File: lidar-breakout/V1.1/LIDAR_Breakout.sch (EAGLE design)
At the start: 88 parts, among them J1 UX60-MB-5S8, P1 MOLEX 0436500200, X1 TSX-3225 16.0000MF18X-AC0

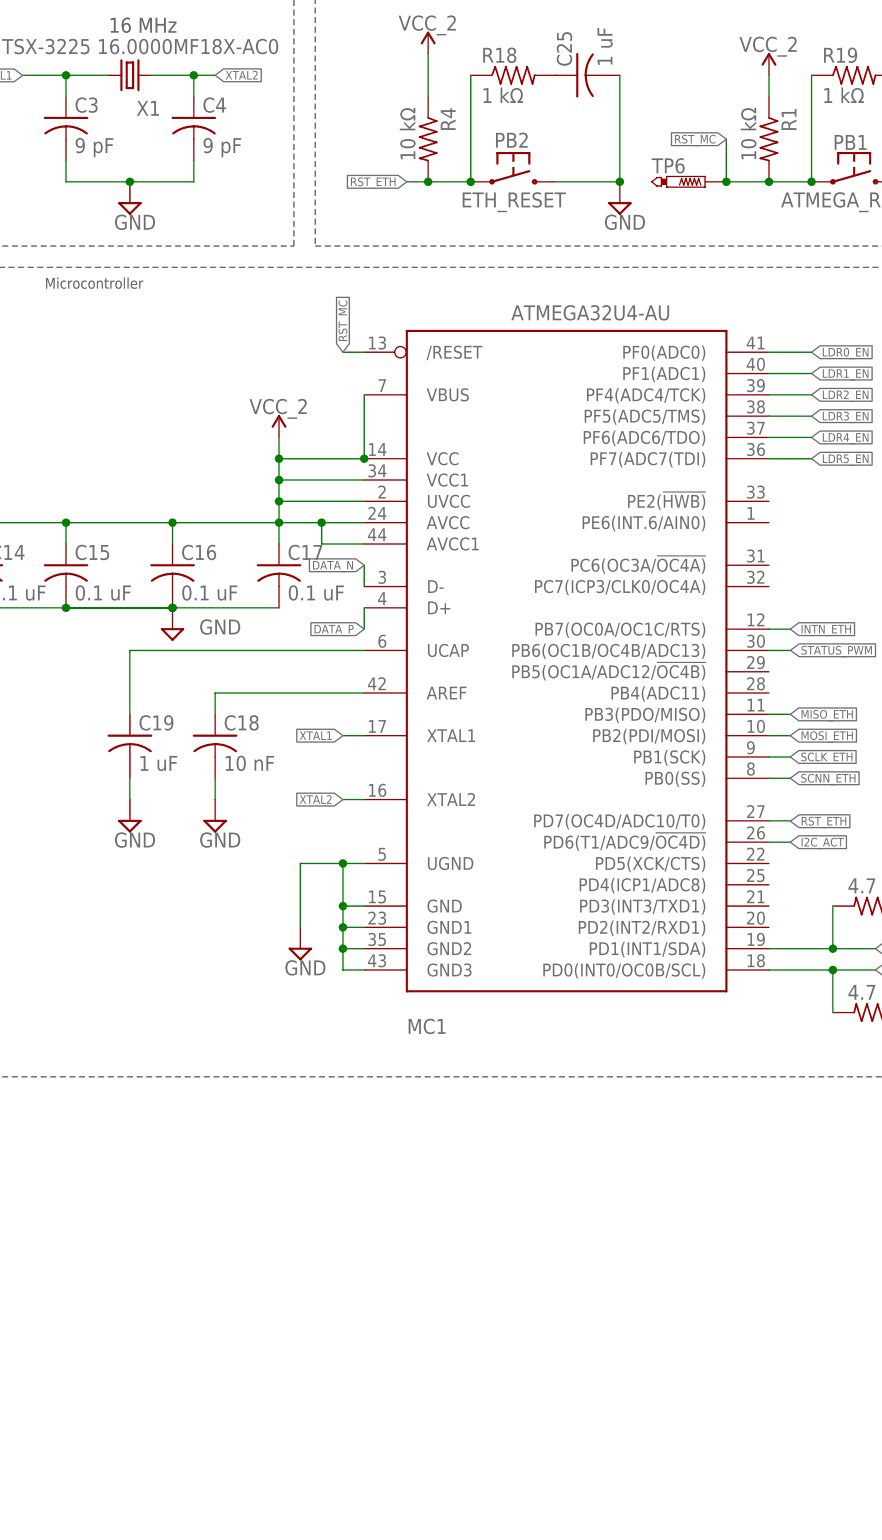
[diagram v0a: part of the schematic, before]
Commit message: Added POGO Pads
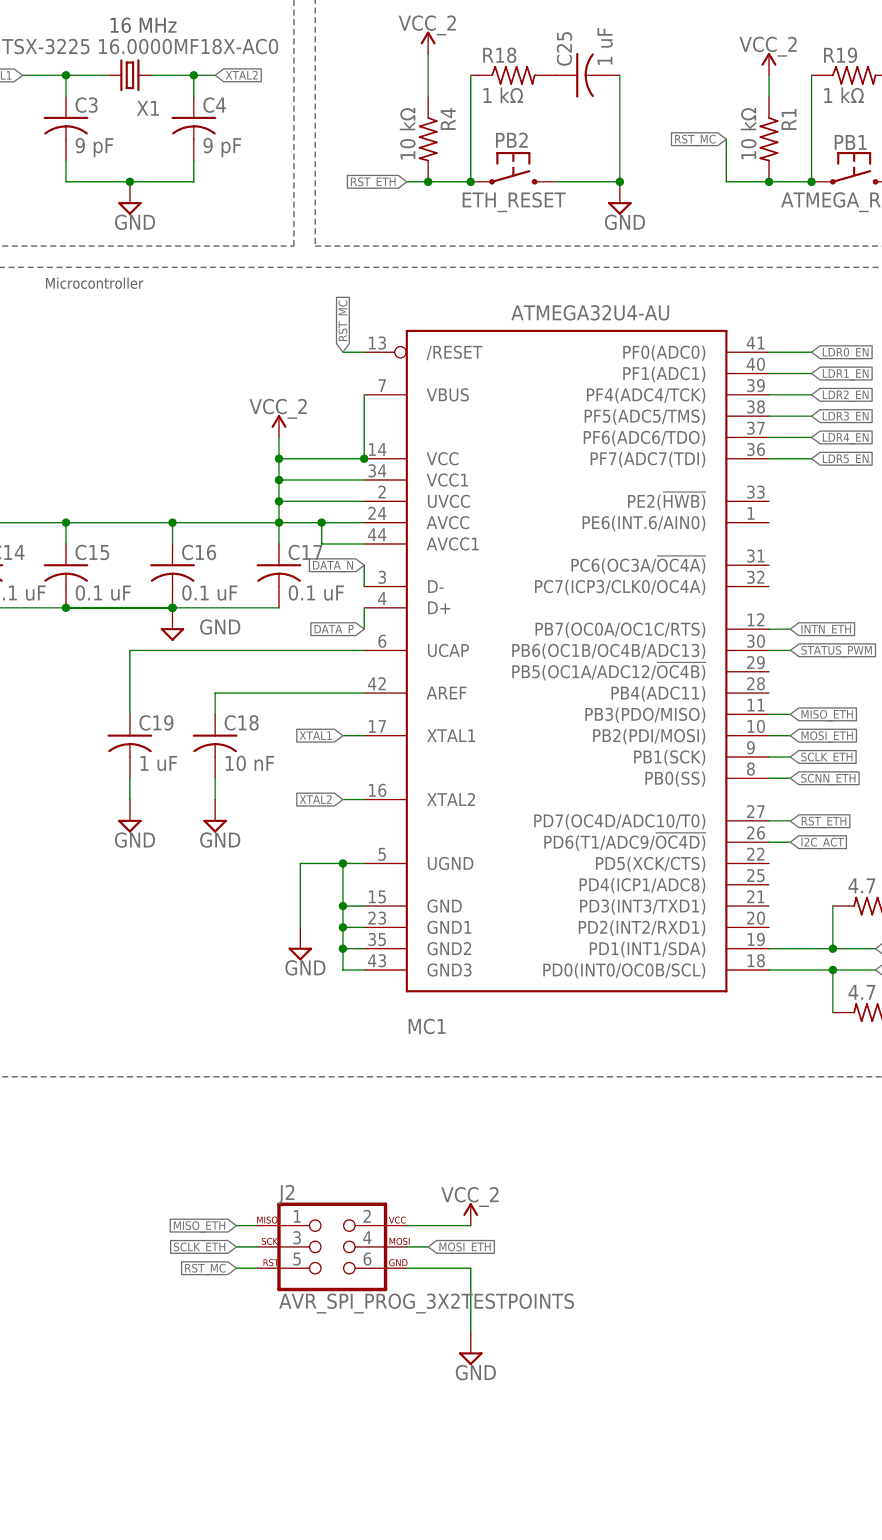
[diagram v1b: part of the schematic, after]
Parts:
- removed TP6: PTR1PAD1-13, testpad:PTR1PAD1-13
- added J2: AVR_SPI_PROG_3X2TESTPOINTS, SparkFun-Connectors:AVR_SPI_PROG_3X2TESTPOINTS
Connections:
- net GND: now also J2.6
- net MISO_ETH: now also J2.1
- net MOSI_ETH: now also J2.4
- net RST_MC: now also J2.5; no longer TP6.TP
- net SCLK_ETH: now also J2.3
- net VCC_2: now also J2.2
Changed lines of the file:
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@@
 <?xml version="1.0" encoding="utf-8"?>
 <!DOCTYPE eagle SYSTEM "eagle.dtd">
-<eagle version="9.3.0">
+<eagle version="9.2.2">
 <drawing>
 <settings>
@@
 <part name="C25" library="resistor" library_urn="urn:adsk.eagle:library:348" deviceset="C-US" device="C0603" package3d_urn="urn:adsk.eagle:package:26138/1" value="1 uF"/>
 <part name="C26" library="resistor" library_urn="urn:adsk.eagle:library:348" deviceset="C-US" device="C0603" package3d_urn="urn:adsk.eagle:package:26138/1" value="0.1 uF"/>
-<part name="TP6" library="testpad" library_urn="urn:adsk.eagle:library:385" deviceset="PTR1" device="PAD1-13" package3d_urn="urn:adsk.eagle:package:27946/1" value="PTR1PAD1-13"/>
 <part name="H1" library="RoboJackets-Connectors" deviceset="SM06B-GHS" device=""/>
 <part name="H2" library="RoboJackets-Connectors" deviceset="SM06B-GHS" device=""/>
@@
 <part name="R18" library="rcl" library_urn="urn:adsk.eagle:library:334" deviceset="R-US_" device="R0603" package3d_urn="urn:adsk.eagle:package:23555/2" value="1 kΩ"/>
 <part name="R19" library="rcl" library_urn="urn:adsk.eagle:library:334" deviceset="R-US_" device="R0603" package3d_urn="urn:adsk.eagle:package:23555/2" value="1 kΩ"/>
+<part name="J2" library="SparkFun-Connectors" library_urn="urn:adsk.eagle:library:513" deviceset="AVR_SPI_PROG_3X2" device="TESTPOINTS" package3d_urn="urn:adsk.eagle:package:38008/1" value="AVR_SPI_PROG_3X2TESTPOINTS"/>
+<part name="SUPPLY14" library="supply2" library_urn="urn:adsk.eagle:library:372" deviceset="GND" device=""/>
+<part name="SUPPLY22" library="SparkFun-PowerSymbols" library_urn="urn:adsk.eagle:library:530" deviceset="VCC_2" device=""/>
 </parts>
 <sheets>
@@
 <attribute name="VALUE" x="258.191" y="244.856" size="1.778" layer="96" rot="R90"/>
 </instance>
-<instance part="TP6" gate="G$1" x="228.6" y="231.14" smashed="yes" rot="R270">
-<attribute name="NAME" x="222.25" y="232.156" size="1.778" layer="95"/>
-<attribute name="TP_SIGNAL_NAME" x="226.06" y="229.87" size="1.778" layer="97" rot="R270"/>
-</instance>
 <instance part="H1" gate="G$1" x="302.26" y="152.4" smashed="yes" rot="MR0">
 <attribute name="NAME" x="307.34" y="170.18" size="1.778" layer="95" font="vector" rot="MR0" align="top-left"/>
@@
 <attribute name="NAME" x="242.57" y="245.3386" size="1.778" layer="95"/>
 <attribute name="VALUE" x="242.57" y="240.538" size="1.778" layer="96"/>
+</instance>
+<instance part="J2" gate="G$1" x="182.88" y="104.14" smashed="yes">
+<attribute name="NAME" x="177.8" y="109.728" size="1.778" layer="95" font="vector"/>
+<attribute name="VALUE" x="177.8" y="96.774" size="1.778" layer="96" font="vector"/>
+</instance>
+<instance part="SUPPLY14" gate="GND" x="200.66" y="91.44" smashed="yes">
+<attribute name="VALUE" x="198.755" y="88.265" size="1.778" layer="96"/>
+</instance>
+<instance part="SUPPLY22" gate="G$1" x="200.66" y="106.68" smashed="yes">
+<attribute name="VALUE" x="200.66" y="109.474" size="1.778" layer="96" align="bottom-center"/>
 </instance>
 </instances>
@@
 <junction x="292.1" y="193.04"/>
 </segment>
+<segment>
+<pinref part="J2" gate="G$1" pin="6"/>
+<wire x1="193.04" y1="101.6" x2="200.66" y2="101.6" width="0.1524" layer="91"/>
+<pinref part="SUPPLY14" gate="GND" pin="GND"/>
+<wire x1="200.66" y1="101.6" x2="200.66" y2="93.98" width="0.1524" layer="91"/>
+</segment>
 </net>
 <net name="RST_MC" class="0">
@@
 <wire x1="231.14" y1="231.14" x2="236.22" y2="231.14" width="0.1524" layer="91"/>
 <junction x="236.22" y="231.14"/>
-<pinref part="TP6" gate="G$1" pin="TP"/>
-<junction x="231.14" y="231.14"/>
 <wire x1="241.3" y1="231.14" x2="241.3" y2="243.84" width="0.1524" layer="91"/>
 <junction x="241.3" y="231.14"/>
@@
 <wire x1="187.96" y1="210.82" x2="185.42" y2="210.82" width="0.1524" layer="91"/>
 <label x="185.42" y="210.82" size="1.016" layer="95" rot="R90" xref="yes"/>
+</segment>
+<segment>
+<pinref part="J2" gate="G$1" pin="5"/>
+<wire x1="175.26" y1="101.6" x2="172.72" y2="101.6" width="0.1524" layer="91"/>
+<label x="172.72" y="101.6" size="1.016" layer="95" rot="R180" xref="yes"/>
 </segment>
 </net>
@@
 <label x="238.76" y="165.1" size="1.016" layer="95" xref="yes"/>
 </segment>
+<segment>
+<pinref part="J2" gate="G$1" pin="4"/>
+<wire x1="193.04" y1="104.14" x2="195.58" y2="104.14" width="0.1524" layer="91"/>
+<label x="195.58" y="104.14" size="1.016" layer="95" xref="yes"/>
+</segment>
 </net>
 <net name="MISO_ETH" class="0">
@@
 <wire x1="236.22" y1="167.64" x2="238.76" y2="167.64" width="0.1524" layer="91"/>
 <label x="238.76" y="167.64" size="1.016" layer="95" xref="yes"/>
+</segment>
+<segment>
+<pinref part="J2" gate="G$1" pin="1"/>
+<wire x1="175.26" y1="106.68" x2="172.72" y2="106.68" width="0.1524" layer="91"/>
+<label x="172.72" y="106.68" size="1.016" layer="95" rot="R180" xref="yes"/>
 </segment>
 </net>
@@
 <pinref part="SUPPLY9" gate="G$1" pin="VCC_2"/>
 </segment>
+<segment>
+<pinref part="J2" gate="G$1" pin="2"/>
+<wire x1="193.04" y1="106.68" x2="200.66" y2="106.68" width="0.1524" layer="91"/>
+<pinref part="SUPPLY22" gate="G$1" pin="VCC_2"/>
+</segment>
 </net>
 <net name="STATUS_PWM" class="0">
@@
 <label x="238.76" y="162.56" size="1.016" layer="95" xref="yes"/>
 </segment>
-</net>
+<segment>
+<pinref part="J2" gate="G$1" pin="3"/>
+<wire x1="175.26" y1="104.14" x2="172.72" y2="104.14" width="0.1524" layer="91"/>
+<label x="172.72" y="104.14" size="1.016" layer="95" rot="R180" xref="yes"/>
+</segment>
+</net>

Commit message: Updated Reset PB
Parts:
- PB1: device RoboJackets-Switches:RESET_PB_RA -> RoboJackets-Switches:PB_RA
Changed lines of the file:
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@@
 <part name="C12" library="resistor" library_urn="urn:adsk.eagle:library:348" deviceset="C-US" device="C0603" package3d_urn="urn:adsk.eagle:package:26138/1" value="0.1 uF"/>
 <part name="C13" library="680uF_Elect_Cap" deviceset="EEE-FTJ681XAP" device="" value="680 uF"/>
-<part name="PB1" library="RoboJackets-Switches" deviceset="RESET_PB_RA" device="" value="ATMEGA_RESET"/>
+<part name="PB1" library="RoboJackets-Switches" deviceset="PB_RA" device="" value="ATMEGA_RESET"/>
 <part name="TP1" library="testpad" library_urn="urn:adsk.eagle:library:385" deviceset="PTR1" device="B1,27" package3d_urn="urn:adsk.eagle:package:27944/1" value="PTR1B1,27"/>
 <part name="TP2" library="testpad" library_urn="urn:adsk.eagle:library:385" deviceset="PTR1" device="B1,27" package3d_urn="urn:adsk.eagle:package:27944/1" value="PTR1B1,27"/>
